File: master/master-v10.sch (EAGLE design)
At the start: 20 parts, among them IC2 DS3231/SO, J1 AVR_SPI_PRG_6PTH, U2 ATMEGA640/1280/2560-A, U3 FT232RL-BASICSSOP

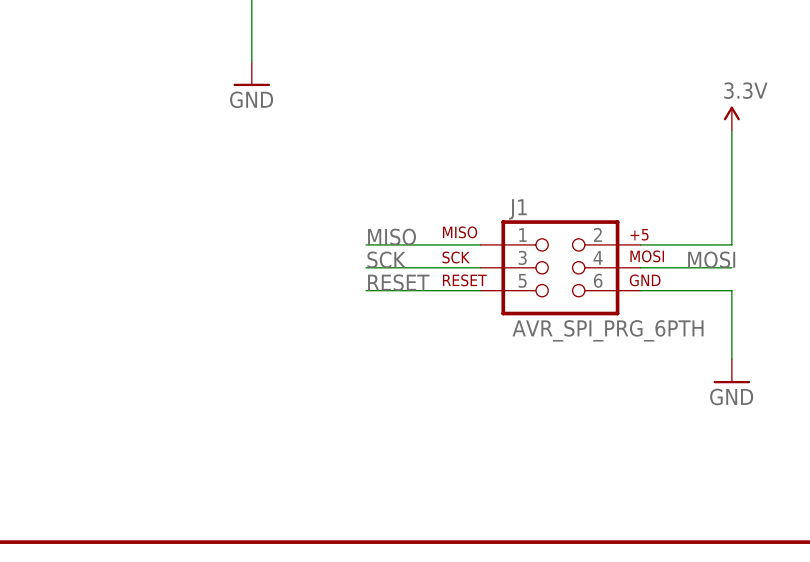
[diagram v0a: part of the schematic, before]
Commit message: fix RESET pin
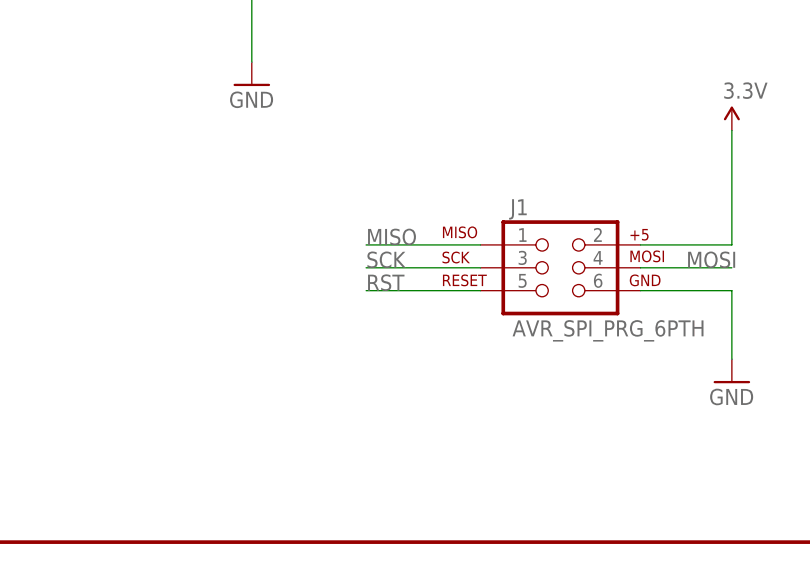
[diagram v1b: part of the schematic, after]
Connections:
- removed net RESET: J1.5
- net RST: now also J1.5
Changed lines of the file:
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@@
 <junction x="157.48" y="215.9"/>
+</segment>
+<segment>
+<pinref part="J1" gate="G$1" pin="5"/>
+<wire x1="180.34" y1="27.94" x2="167.64" y2="27.94" width="0.1524" layer="91"/>
+<label x="167.64" y="27.94" size="1.778" layer="95"/>
 </segment>
 </net>
@@
 </segment>
 </net>
-<net name="RESET" class="0">
-<segment>
-<pinref part="J1" gate="G$1" pin="5"/>
-<wire x1="180.34" y1="27.94" x2="167.64" y2="27.94" width="0.1524" layer="91"/>
-<label x="167.64" y="27.94" size="1.778" layer="95"/>
-</segment>
-</net>

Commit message: Avanzado diagrama de la parte del ft232.
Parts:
- removed FRAME1: FRAME-LEDGER, SparkFun-Aesthetics:FRAME-LEDGER
- added C8: 10uF, rcl:C-EUC1206K
- added C9: 0.1uF, rcl:C-EUC0805K
- added R2, R5: 1k, rcl:R-EU_R0805
- added R6, R7: 10, rcl:R-EU_R0805
- added RX_L: Green, led:LEDSML0805
- added TX_L: Red, led:LEDSML0805
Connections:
- removed net N$5: LED2.C, U2.AREF, U2.AVCC, U2.VCC@1, U2.VCC@2, U2.VCC@3, U2.VCC@4
- removed net RXD: U2.(PCINT8/RXD0)PE0
- removed net TXD: U2.(TXD0)PE1
- new net N$10: RX_L.C, U3.RXLED
- new net N$11: R7.1, RX_L.A
- new net N$12: TX_L.C, U3.TXLED
- new net N$13: R6.1, TX_L.A
- new net N$14: U2.PH0(RXD2)
- new net N$15: U2.PJ1(TXD3/PCINT10)
- new net N$16: U2.PJ0(RXD3/PCINT9)
- new net N$17: U2.(TXD1/INT3)PD3
- new net N$18: U2.(RXD1/INT2)PD2
- new net N$2: U2.PH1(TXD2)
- new net N$6: R2.1, U3.TXD
- new net N$8: R5.1, U3.RXD
- new net RX_FT232: R5.2, U2.(TXD0)PE1
- new net TX_FT232: R2.2, U2.(PCINT8/RXD0)PE0
- new net USB_D+: U3.USBDP
- new net USB_D-: U3.USBDM
- net 3.3V: now also C8.1, C9.1, R6.2, R7.2, U2.AREF, U2.AVCC, U2.VCC@1, U2.VCC@2, U2.VCC@3, U2.VCC@4, U3.VCC
- net DTR: now also U3.DTR
- net GND: now also C8.2, C9.2, LED2.C, U3.AGND, U3.CTS, U3.GND1, U3.GND2, U3.GND3, U3.TEST
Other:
- moved on the sheet: LED2, R3, U3

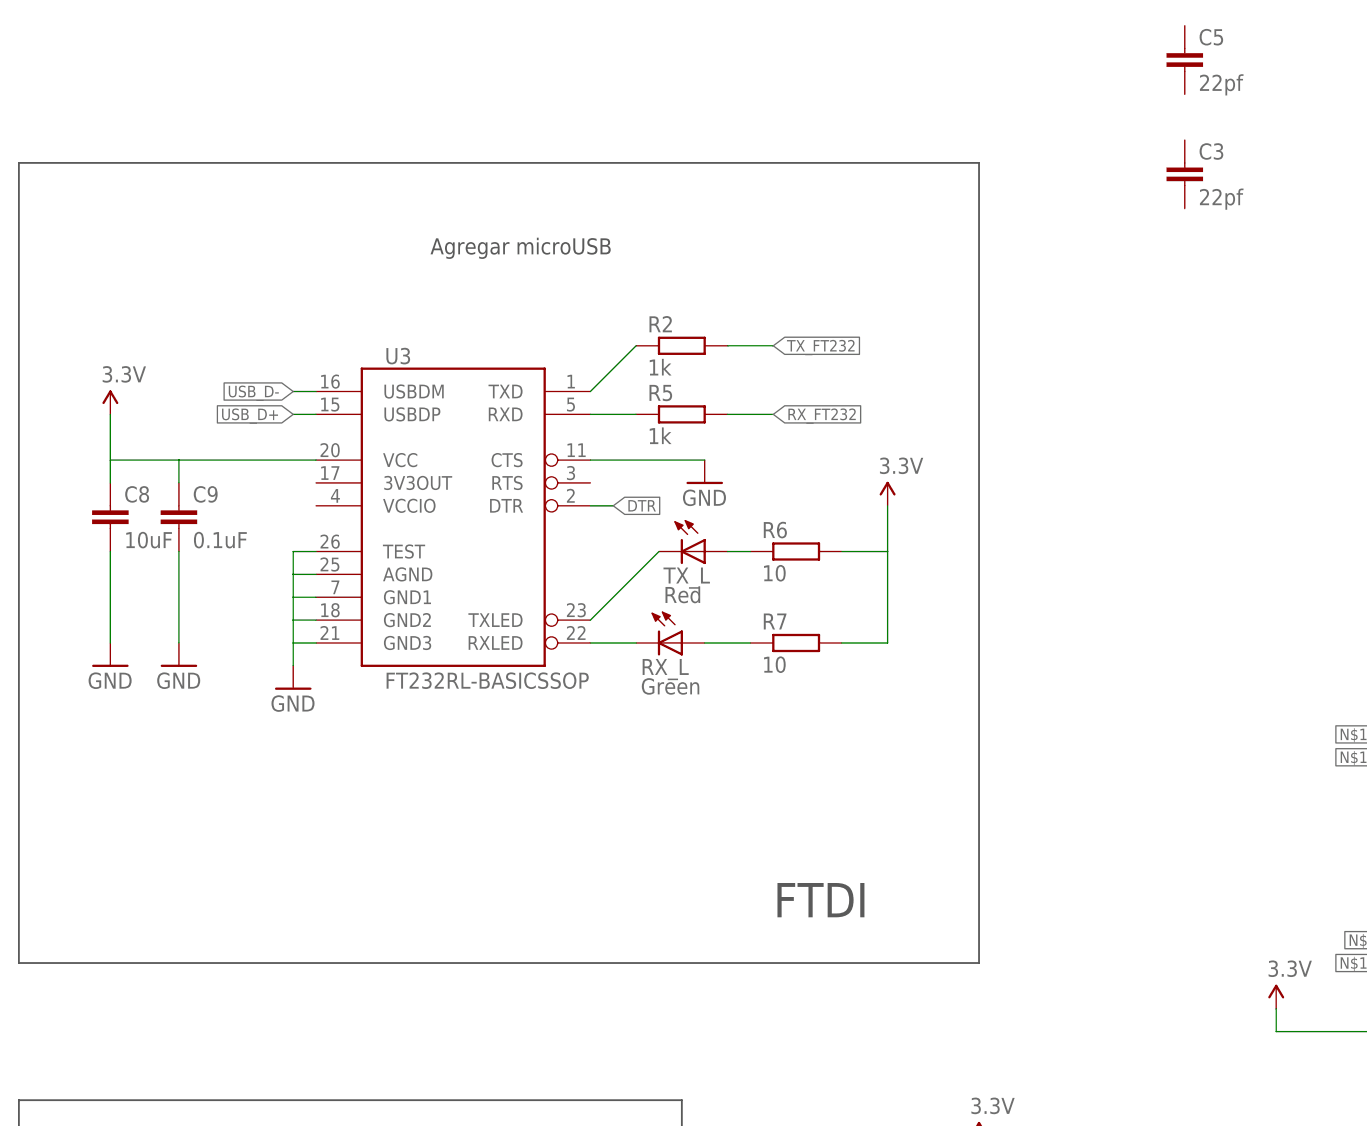
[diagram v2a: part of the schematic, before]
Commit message: Conector USBMini
Es más resistente que el USBmicro mecanicamente. El usb normal exije un
cable no tan standar
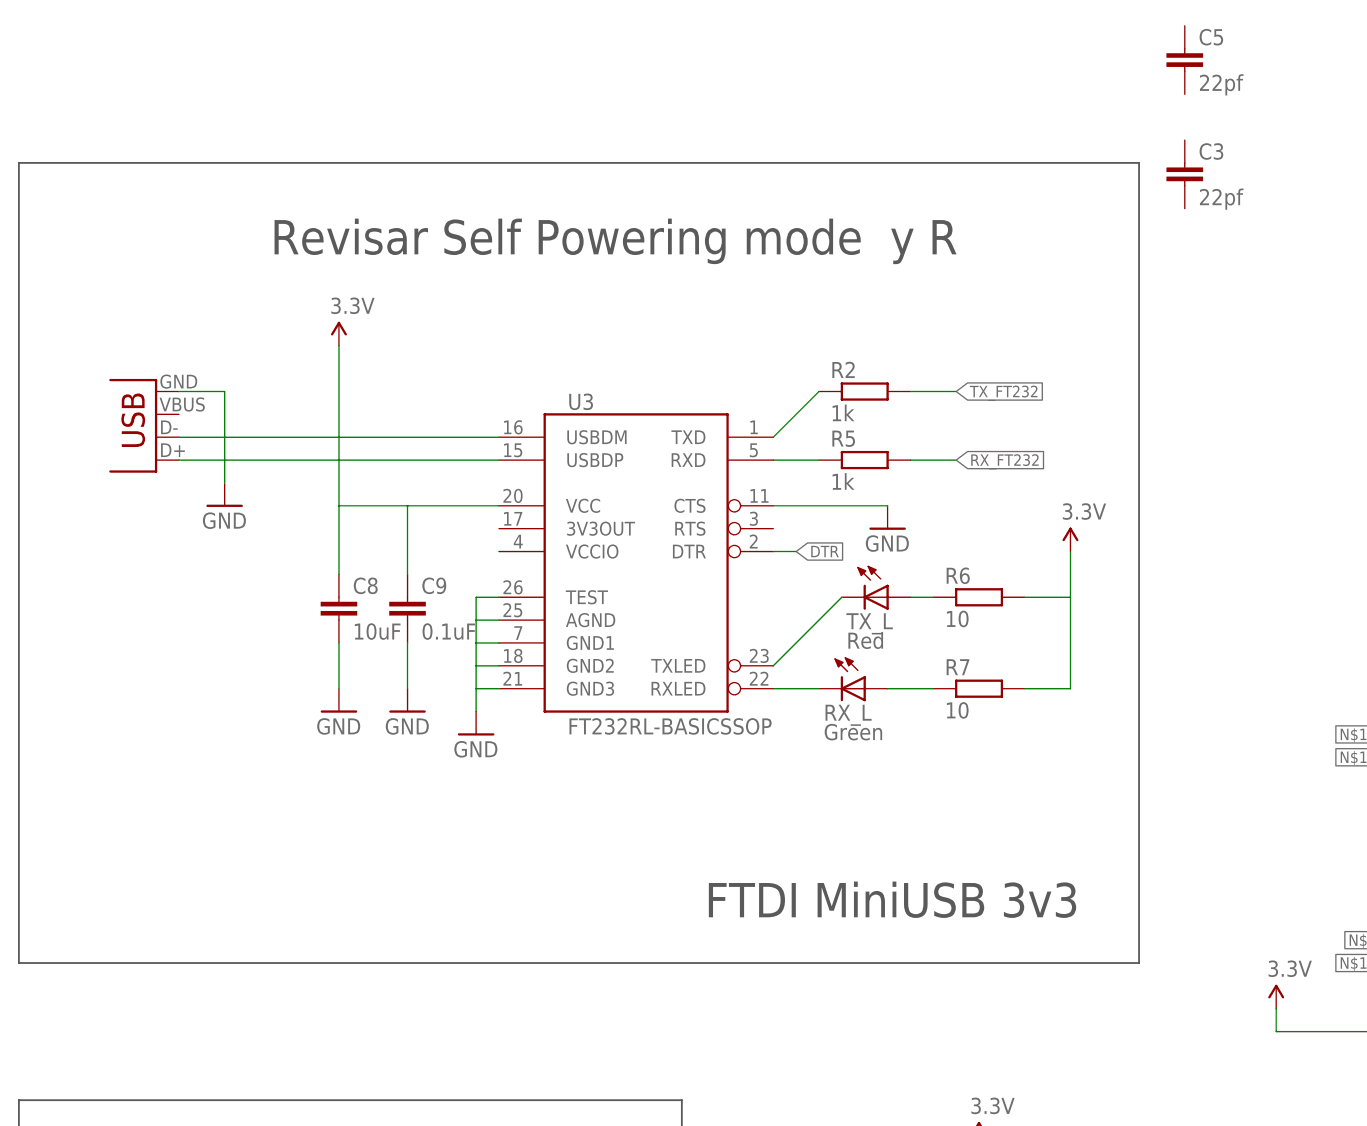
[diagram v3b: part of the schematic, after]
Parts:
- added JP1: USB-MB-H, SparkFun-Connectors:USB-MB-H
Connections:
- removed net USB_D+: U3.USBDP
- removed net USB_D-: U3.USBDM
- new net N$19: JP1.D-, U3.USBDM
- new net N$5: JP1.D+, U3.USBDP
- net GND: now also JP1.GND
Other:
- note added: "FTDI MiniUSB 3v3"
- note added: "Revisar Self Powering mode y R"
- note removed: "Agregar microUSB"
- note removed: "FTDI"
- moved on the sheet: C8, C9, R2, R5, R6, R7, RX_L, TX_L, U3

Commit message: todos los componentes V10
Falta revisar compatibilidad entre modulos y hacer layout
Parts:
- removed U$1: MICROSD-HRS_DM3D, hrs_DM3D-SF:MICROSD-HRS_DM3D
- added C10: 0.1uF, SparkFun:CAP0402-CAP
- added FRAME1: FRAME-LEDGER, SparkFun-Aesthetics:FRAME-LEDGER
- added IC1: DS1820, DS1820:DS1820
- added LED3, LED4: (no value), adafruit:LEDCHIPLED_0805
- added R10: 4k7, SparkFun:RESISTOR0402-RES
- added R11: 1k, SparkFun:RESISTOR0402-RES
- added R12: 0.002, SparkFun-Resistors:RESISTOR1206
- added R8: 220, SparkFun:RESISTOR0402-RES
- added R9: 1K, SparkFun:RESISTOR0402-RES
- added U$2: RS485SOIC, SparkFun-DigitalIC:RS485SOIC
- added U4: AP1117E, v-reg:AP1117E
- added U5: USD-SOCKETNEW, SparkFun-Connectors:USD-SOCKETNEW
- added Y1: (no value), SparkFun-FreqCtrl:CRYSTALHC49US
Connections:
- new net A: R8.2, U$2.A
- new net B: R8.1, U$2.B
- new net N$20: LED3.A, R9.2
- new net N$21: C5.1, U2.XTAL1, Y1.2
- new net N$22: C3.2, U2.XTAL2, Y1.1
- new net N$23: LED4.A, R11.2
- new net RTS: R9.1, U$2./RE, U$2.DE
- new net RX-I: U$2.DI
- new net TEMP: IC1.DQ, R10.2
- new net TX-O: U$2.RO
- net 3.3V: now also C10.1, IC1.VDD, R10.1, U$2.VCC, U4.OUT, U5.VCC
- net CS: now also U5.CS
- net GND: now also C10.2, C3.1, C5.2, IC1.GND, LED3.C, LED4.C, U$2.GND, U4.GND, U5.GND, U5.SHIELD@1, U5.SHIELD@3
- net MISO: now also U5.DO
- net MOSI: now also U5.DI
- net RAW: now also U4.IN
- net SCK: now also R11.1, U5.SCK
- net VIN+: now also R12.2
- net VIN-: now also R12.1
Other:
- note added: "Hacer conexion a Atmega UART2 y agregar terminal"
- note added: "Max Current Output: 1A"
- note added: "Max Voltage Input: 18VDC"
- note added: "RS485"
- note added: "Regulador 12V -> 3v3"
- note removed: "Max Current Output: ?mA"
- note removed: "Max Voltage Input: ?VDC"
- note removed: "Regulador 12V -"
- moved on the sheet: C1, C2, C3, C5, C7, C8, C9, J1, LED1, LED2, R1, R2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

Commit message: arrelado problema del ftdi
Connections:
- new net N$24: C8.1, C9.1, JP1.VBUS, U3.VCC
- new net N$25: U3.3V3OUT, U3.VCCIO
- net 3.3V: no longer C8.1, C9.1, U3.VCC
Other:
- note removed: "Revisar Self Powering mode y R"
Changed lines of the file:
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@@
 <part name="TX_L" library="led" deviceset="LED" device="SML0805" value="Red"/>
 <part name="SUPPLY7" library="SparkFun-Aesthetics" deviceset="3.3V" device=""/>
-<part name="SUPPLY8" library="SparkFun-Aesthetics" deviceset="3.3V" device=""/>
 <part name="GND12" library="SparkFun" deviceset="GND" device=""/>
 <part name="SUPPLY9" library="SparkFun-Aesthetics" deviceset="3.3V" device=""/>
@@
 <wire x1="281.94" y1="43.18" x2="281.94" y2="114.3" width="0.2032" layer="97"/>
 <text x="360.68" y="45.72" size="3.81" layer="97">tarjeta MicroSD</text>
-<text x="30.48" y="185.42" size="3.81" layer="97">Revisar Self Powering mode  y R</text>
 <wire x1="281.94" y1="215.9" x2="411.48" y2="215.9" width="0.2032" layer="97"/>
 <wire x1="411.48" y1="215.9" x2="411.48" y2="162.56" width="0.2032" layer="97"/>
@@
 <instance part="TX_L" gate="G$1" x="91.44" y="144.78" rot="R270"/>
 <instance part="SUPPLY7" gate="G$1" x="111.76" y="149.86"/>
-<instance part="SUPPLY8" gate="G$1" x="30.48" y="172.72"/>
 <instance part="GND12" gate="1" x="91.44" y="152.4"/>
 <instance part="SUPPLY9" gate="G$1" x="160.02" y="116.84"/>
@@
 </segment>
 <segment>
-<pinref part="U3" gate="G$1" pin="VCC"/>
-<wire x1="48.26" y1="154.94" x2="38.1" y2="154.94" width="0.1524" layer="91"/>
-<pinref part="C8" gate="G$1" pin="1"/>
-<wire x1="38.1" y1="154.94" x2="30.48" y2="154.94" width="0.1524" layer="91"/>
-<wire x1="30.48" y1="154.94" x2="30.48" y2="147.32" width="0.1524" layer="91"/>
-<pinref part="C9" gate="G$1" pin="1"/>
-<wire x1="38.1" y1="154.94" x2="38.1" y2="147.32" width="0.1524" layer="91"/>
-<pinref part="SUPPLY8" gate="G$1" pin="3.3V"/>
-<wire x1="30.48" y1="172.72" x2="30.48" y2="154.94" width="0.1524" layer="91"/>
-</segment>
-<segment>
 <pinref part="U2" gate="G$1" pin="VCC@1"/>
 <wire x1="175.26" y1="124.46" x2="172.72" y2="124.46" width="0.1524" layer="91"/>
@@
 </segment>
 </net>
+<net name="N$24" class="0">
+<segment>
+<pinref part="U3" gate="G$1" pin="VCC"/>
+<wire x1="48.26" y1="154.94" x2="38.1" y2="154.94" width="0.1524" layer="91"/>
+<pinref part="C8" gate="G$1" pin="1"/>
+<wire x1="38.1" y1="154.94" x2="30.48" y2="154.94" width="0.1524" layer="91"/>
+<wire x1="30.48" y1="154.94" x2="30.48" y2="147.32" width="0.1524" layer="91"/>
+<pinref part="C9" gate="G$1" pin="1"/>
+<wire x1="38.1" y1="154.94" x2="38.1" y2="147.32" width="0.1524" layer="91"/>
+<pinref part="JP1" gate="G$1" pin="VBUS"/>
+<wire x1="30.48" y1="165.1" x2="30.48" y2="154.94" width="0.1524" layer="91"/>
+<wire x1="12.7" y1="165.1" x2="30.48" y2="165.1" width="0.1524" layer="91"/>
+</segment>
+</net>
+<net name="N$25" class="0">
+<segment>
+<pinref part="U3" gate="G$1" pin="3V3OUT"/>
+<wire x1="48.26" y1="152.4" x2="45.72" y2="152.4" width="0.1524" layer="91"/>
+<wire x1="45.72" y1="152.4" x2="45.72" y2="149.86" width="0.1524" layer="91"/>
+<pinref part="U3" gate="G$1" pin="VCCIO"/>
+<wire x1="45.72" y1="149.86" x2="48.26" y2="149.86" width="0.1524" layer="91"/>
+</segment>
+</net>

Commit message: avanzado temperatura y otros
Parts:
- removed IC1: DS1820, DS1820:DS1820
- added J2: TWIG-2.0-DIPD, Grove :TWIG-2.0-DIPD
- added R13: 82k, SparkFun:RESISTOR0402-RES
- added R14, R16: 10k, SparkFun:RESISTOR0402-RES
- added R15: 3.3k, SparkFun:RESISTOR0402-RES
- added U6: INA169, SparkFun-AnalogIC:INA169
- R10: value 4k7 -> 10k
- U1: value (none) -> MCP9804; device microbuilder:INA219 -> MCP9804:MCP9804
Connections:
- removed net CS: U2.(!SS!/PCINT0)PB0, U5.CS
- removed net N$14: U2.PH0(RXD2)
- removed net N$2: U2.PH1(TXD2)
- removed net SCL: IC2.SCL, U1.SCL
- removed net SDA: IC2.SDA, U1.SDA
- removed net TEMP: IC1.DQ, R10.2
- new net CS_SD: U2.(ADC2)PF2, U5.CS
- new net N$27: U1.A1
- new net RX_GPS: J2.2, U2.PH1(TXD2)
- new net SENSOR_CURRENT: C7.1, R13.2, U2.(ADC0)PF0, U6.OUT
- new net SENSOR_VOLT: R14.2, R15.2, U2.(ADC1)PF1
- new net TX_GPS: J2.3, U2.PH0(RXD2)
- net 3.3V: now also J2.4, R16.1, U1.VDD, U6.V+; no longer C7.1, IC1.VDD, U1.VCC
- net GND: now also J2.1, R13.1, R15.1, U1.A2, U6.GND; no longer IC1.GND, U1.A1
- net MOSI: now also IC2.SDA, R16.2, U1.SDA
- net RAW: now also R14.1
- net SCK: now also IC2.SCL, R10.2, U1.SCK
- net VIN+: now also U6.VIN+; no longer U1.VIN+
- net VIN-: now also U6.VIN-; no longer U1.VIN-
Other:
- note added: "GPS"
- moved on the sheet: C7, R10, R12

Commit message: agregado comunicacion
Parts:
- removed C10: 0.1uF, SparkFun:CAP0402-CAP
- removed LED3: (no value), adafruit:LEDCHIPLED_0805
- removed R8: 220, SparkFun:RESISTOR0402-RES
- removed R9: 1K, SparkFun:RESISTOR0402-RES
- removed U$2: RS485SOIC, SparkFun-DigitalIC:RS485SOIC
- added J3, J4: TWIG-2.0-DIPD, Grove :TWIG-2.0-DIPD
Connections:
- removed net A: R8.2, U$2.A
- removed net B: R8.1, U$2.B
- removed net N$15: U2.PJ1(TXD3/PCINT10)
- removed net N$16: U2.PJ0(RXD3/PCINT9)
- removed net N$17: U2.(TXD1/INT3)PD3
- removed net N$18: U2.(RXD1/INT2)PD2
- removed net N$20: LED3.A, R9.2
- removed net RTS: R9.1, U$2./RE, U$2.DE
- removed net RX-I: U$2.DI
- removed net TX-O: U$2.RO
- new net BT_RX: J4.2, U2.PJ1(TXD3/PCINT10)
- new net BT_TX: J4.3, U2.PJ0(RXD3/PCINT9)
- new net COMM_RX: J3.2, U2.(TXD1/INT3)PD3
- new net COMM_TX: J3.3, U2.(RXD1/INT2)PD2
- net 3.3V: now also J4.4; no longer C10.1, U$2.VCC
- net GND: now also J3.1, J4.1; no longer C10.2, LED3.C, U$2.GND
- net RAW: now also J3.4
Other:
- note added: "Comunicacion"
- note removed: "Hacer conexion a Atmega UART2 y agregar terminal"
- note removed: "RS485"
